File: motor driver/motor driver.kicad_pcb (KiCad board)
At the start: 2 copper layers, 105.4 x 72.4 mm, 49 parts, among them J1 M1, J2 M3, J3 JST IN, J5 M2, J6 M4, J7 Solar Connector, U1 L298HN, U2 L298HN, U3 L7805, U4 74HC04

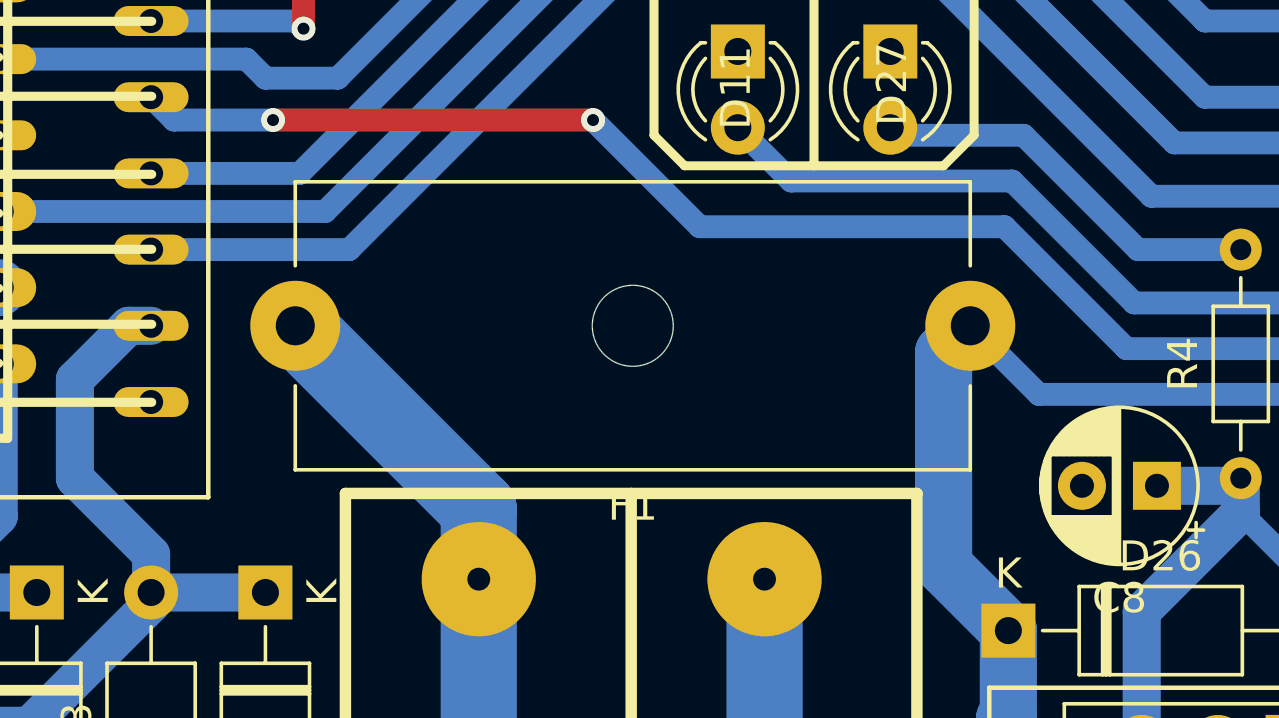
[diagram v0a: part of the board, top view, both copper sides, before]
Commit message: mega shield sch done
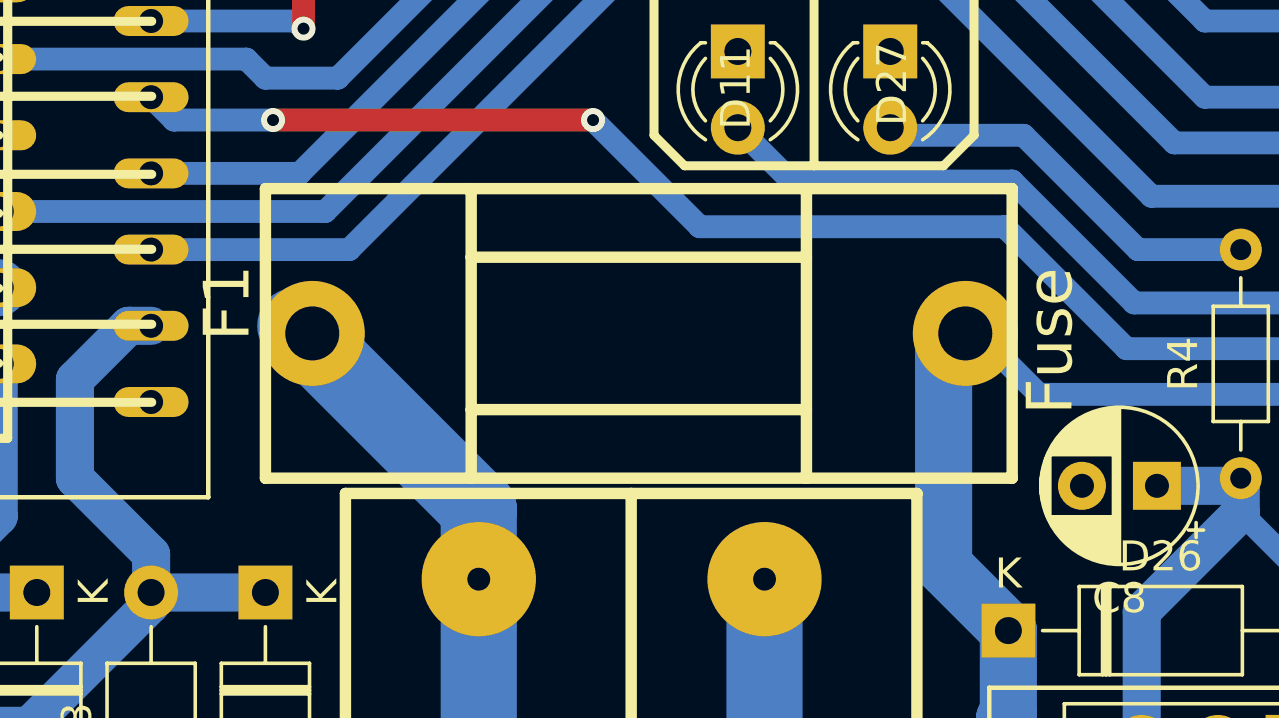
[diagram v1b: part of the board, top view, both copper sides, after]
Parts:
- F1: footprint Fuse:Fuseholder_Cylinder-5x20mm_Schurter_0031_8201_Horizontal_Open -> rashik:fuse_holder
- moved F1 11.1 mm to (115.3, 100.6), turned to 270 degrees

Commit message: motor driver done
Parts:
- removed C9: 220uF, Capacitor_THT:CP_Radial_D5.0mm_P2.50mm
- removed J7: Solar Connector, rashik:Screw_Terminal_2_Pin
- removed U3: L7805, rashik:TO-220-3_Vertical
- added J4: Solar Conn, rashik:Screw_Terminal_3_Pin, F.Cu at (119.4, 114.9)
- C8: value 10uF -> 100uF
- moved C8 18.3 mm to (141.0, 121.9), turned to 90 degrees
- moved C3 15.1 mm to (138.7, 116.8), turned to 0 degrees
- moved D26 8.35 mm to (135.9, 111.8), turned to 270 degrees
- moved D11 1.41 mm to (120.0, 91.0)
- moved C1 1.17 mm to (103.9, 83.1)
- moved D4 1.02 mm to (92.5, 78.7)
- moved D27 0.79 mm to (124.5, 91.0)
- moved D19 0.51 mm to (102.4, 68.6)
- moved D17 0.51 mm to (90.9, 119.4)
- moved D20 0.51 mm to (95.8, 68.6)
- moved R3 0.51 mm to (80.8, 70.5)
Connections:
- D26 pad 1: +12V -> GND
- D26 pad 2: Net-(C9-Pad1) -> +5V
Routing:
- net +5V: track 112.9 -> 134.2 mm
- net Net-(C9-Pad1): track 9.03 -> 0.00 mm
- net M1-PWM: track 47.3 -> 51.0 mm
- net +12V: track 500.6 -> 497.6 mm
- net M2-PWM: track 36.1 -> 33.7 mm
- net GND: track 23.6 -> 21.5 mm
- net Net-(D11-Pad2): track 23.7 -> 22.2 mm
- net Net-(U1-Pad12): track 32.6 -> 33.7 mm
- net Net-(D27-Pad2): track 13.4 -> 12.7 mm
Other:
- board text added: "AAYAAM TECHNOLOGIES"
- board text removed: "AAYAAM TECHNOLOGY"
